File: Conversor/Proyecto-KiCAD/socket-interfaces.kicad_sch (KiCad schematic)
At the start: 24 parts, among them J7 DIMM100, P10 Header GPIO, P11 Header SD, P5 Header 7X2, P6 Header UART, P7 Header I2C, P8 Header PWM, P9 Header ADC, SW1 Switch, SW2 Switch, SW3 Switch, SW4 Switch

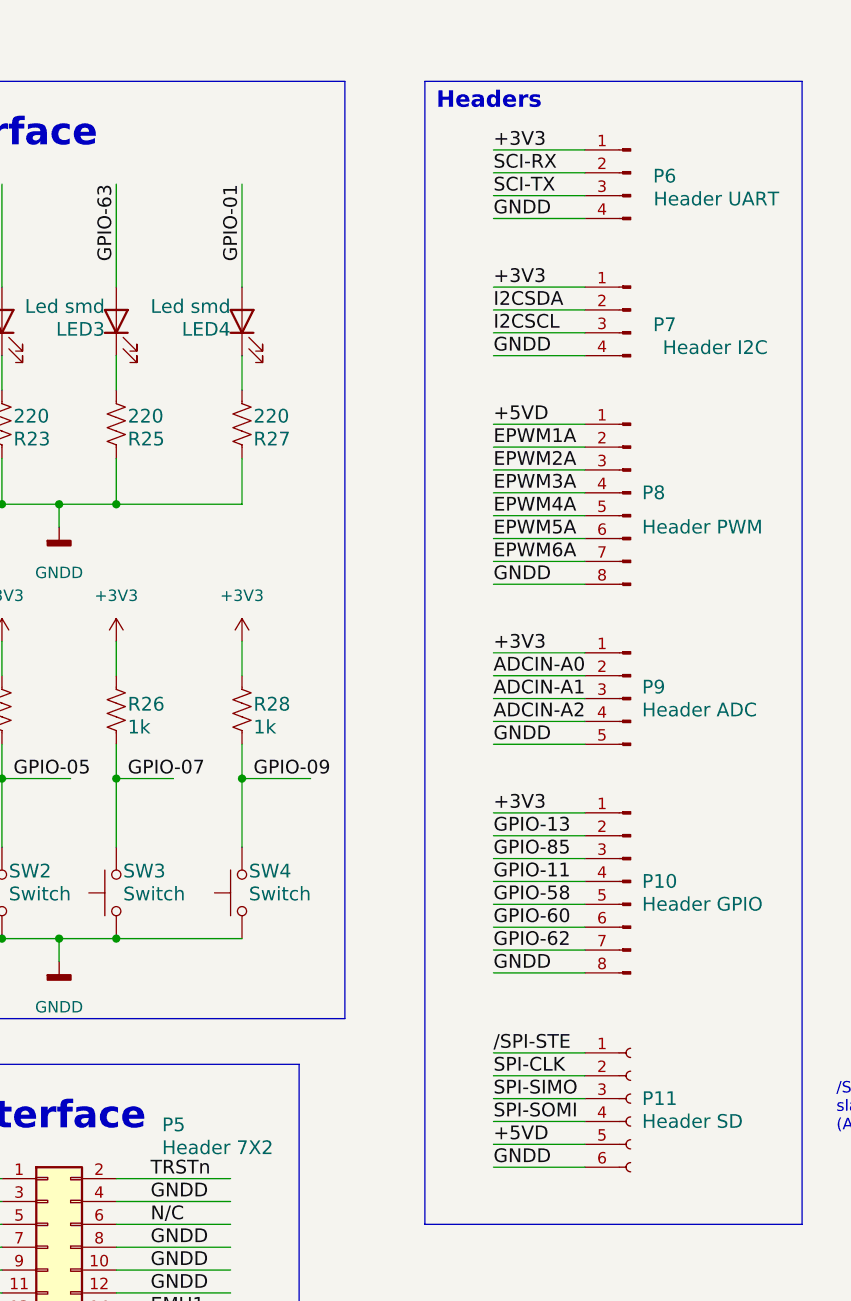
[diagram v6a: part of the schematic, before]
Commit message: Agregar el selector de alim. de 12V y seguir emprolijando la placa
- Agregar modelos de los switches
- Agregar algunos test points
Por hacer:
  - Todo lo de los dos anteriores commits
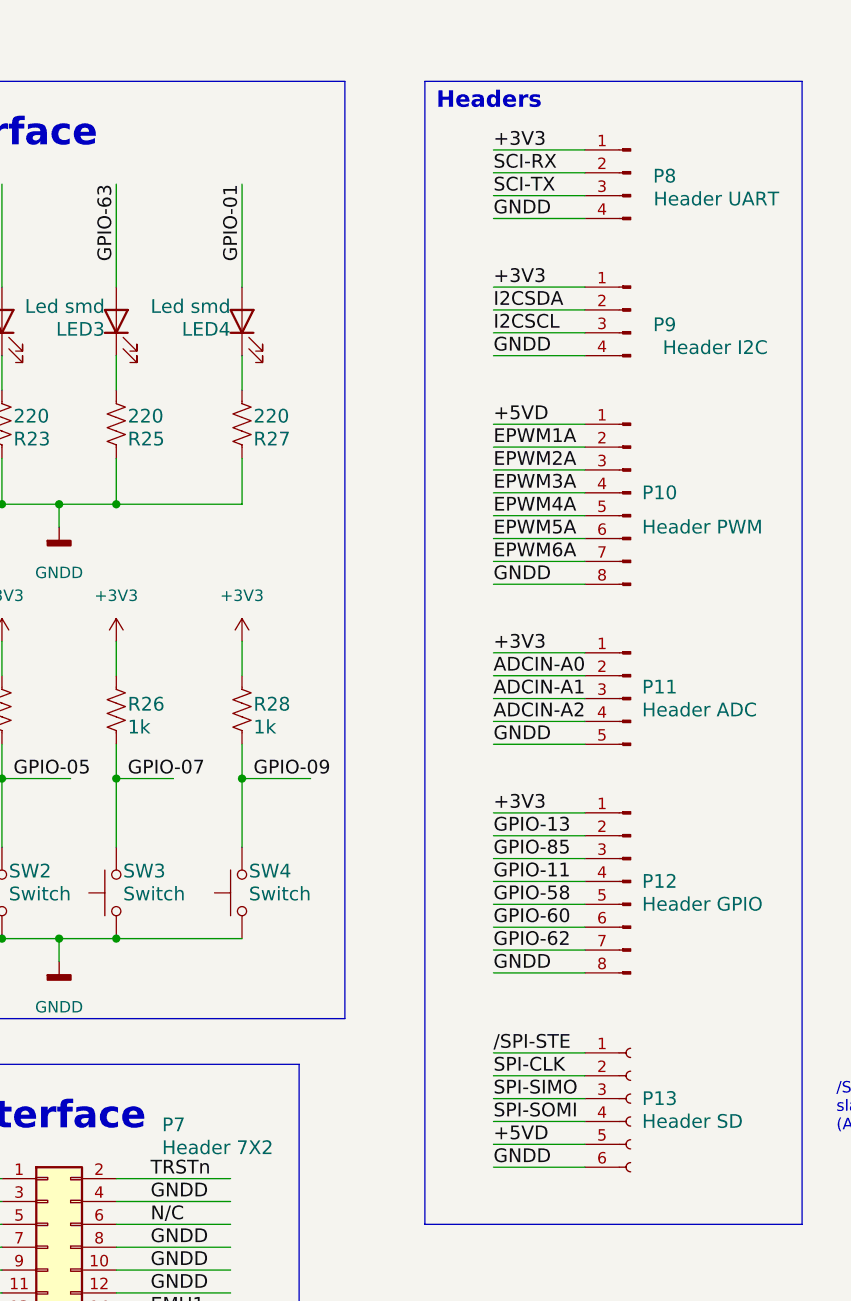
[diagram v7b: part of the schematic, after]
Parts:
- renumbered P8 to P10, P9 to P11, P10 to P12, P11 to P13, P5 to P7, P6 to P8, P7 to P9
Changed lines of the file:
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@@
   (symbol (lib_id "power:+3V3") (at 133.35 90.17 0) (unit 1)
     (in_bom yes) (on_board yes) (fields_autoplaced)
-    (property "Reference" "#PWR0119" (id 0) (at 133.35 93.98 0)
+    (property "Reference" "#PWR080" (id 0) (at 133.35 93.98 0)
       (effects (font (size 1.27 1.27)) hide)
     )
@@
   (symbol (lib_id "power:+3V3") (at 120.65 90.17 0) (unit 1)
     (in_bom yes) (on_board yes) (fields_autoplaced)
-    (property "Reference" "#PWR0144" (id 0) (at 120.65 93.98 0)
+    (property "Reference" "#PWR077" (id 0) (at 120.65 93.98 0)
       (effects (font (size 1.27 1.27)) hide)
     )
@@
   (symbol (lib_id "Connector:Conn_01x04_Male") (at 190.5 38.1 0) (mirror y) (unit 1)
     (in_bom yes) (on_board yes)
-    (property "Reference" "P6" (id 0) (at 195.58 39.37 0)
+    (property "Reference" "P8" (id 0) (at 195.58 39.37 0)
       (effects (font (size 1.524 1.524)) (justify left bottom))
     )
@@
   (symbol (lib_id "Connector_Generic:Conn_02x07_Odd_Even") (at 125.73 157.48 0) (unit 1)
     (in_bom yes) (on_board yes)
-    (property "Reference" "P5" (id 0) (at 138.43 144.78 0)
+    (property "Reference" "P7" (id 0) (at 138.43 144.78 0)
       (effects (font (size 1.524 1.524)) (justify left bottom))
     )
@@
   (symbol (lib_id "power:+3V3") (at 147.32 90.17 0) (unit 1)
     (in_bom yes) (on_board yes) (fields_autoplaced)
-    (property "Reference" "#PWR0121" (id 0) (at 147.32 93.98 0)
+    (property "Reference" "#PWR081" (id 0) (at 147.32 93.98 0)
       (effects (font (size 1.27 1.27)) hide)
     )
@@
   (symbol (lib_id "Connector:Conn_01x04_Male") (at 190.5 53.34 0) (mirror y) (unit 1)
     (in_bom yes) (on_board yes)
-    (property "Reference" "P7" (id 0) (at 195.58 55.88 0)
+    (property "Reference" "P9" (id 0) (at 195.58 55.88 0)
       (effects (font (size 1.524 1.524)) (justify left bottom))
     )
@@
   (symbol (lib_id "Connector:Conn_01x06_Female") (at 190.5 140.97 0) (unit 1)
     (in_bom yes) (on_board yes)
-    (property "Reference" "P11" (id 0) (at 191.77 140.97 0)
+    (property "Reference" "P13" (id 0) (at 191.77 140.97 0)
       (effects (font (size 1.524 1.524)) (justify left))
     )
@@
   (symbol (lib_id "power:GNDD") (at 127 77.47 0) (unit 1)
     (in_bom yes) (on_board yes) (fields_autoplaced)
-    (property "Reference" "#PWR0120" (id 0) (at 127 83.82 0)
+    (property "Reference" "#PWR078" (id 0) (at 127 83.82 0)
       (effects (font (size 1.27 1.27)) hide)
     )
@@
   (symbol (lib_id "Connector:Conn_01x05_Male") (at 190.5 96.52 0) (mirror y) (unit 1)
     (in_bom yes) (on_board yes)
-    (property "Reference" "P9" (id 0) (at 191.77 95.25 0)
+    (property "Reference" "P11" (id 0) (at 191.77 95.25 0)
       (effects (font (size 1.524 1.524)) (justify right))
     )
@@
   (symbol (lib_id "Connector:Conn_01x08_Male") (at 190.5 116.84 0) (mirror y) (unit 1)
     (in_bom yes) (on_board yes)
-    (property "Reference" "P10" (id 0) (at 191.77 116.84 0)
+    (property "Reference" "P12" (id 0) (at 191.77 116.84 0)
       (effects (font (size 1.524 1.524)) (justify right))
     )
@@
   (symbol (lib_id "power:+5VD") (at 251.46 36.83 0) (unit 1)
     (in_bom yes) (on_board yes) (fields_autoplaced)
-    (property "Reference" "#PWR0115" (id 0) (at 251.46 40.64 0)
+    (property "Reference" "#PWR082" (id 0) (at 251.46 40.64 0)
       (effects (font (size 1.27 1.27)) hide)
     )
@@
   (symbol (lib_id "power:GNDD") (at 264.16 40.64 0) (unit 1)
     (in_bom yes) (on_board yes) (fields_autoplaced)
-    (property "Reference" "#PWR0117" (id 0) (at 264.16 46.99 0)
+    (property "Reference" "#PWR084" (id 0) (at 264.16 46.99 0)
       (effects (font (size 1.27 1.27)) hide)
     )
@@
   (symbol (lib_id "power:+3V3") (at 106.68 90.17 0) (unit 1)
     (in_bom yes) (on_board yes) (fields_autoplaced)
-    (property "Reference" "#PWR0122" (id 0) (at 106.68 93.98 0)
+    (property "Reference" "#PWR076" (id 0) (at 106.68 93.98 0)
       (effects (font (size 1.27 1.27)) hide)
     )
@@
   (symbol (lib_id "power:+3V3") (at 257.81 36.83 0) (unit 1)
     (in_bom yes) (on_board yes) (fields_autoplaced)
-    (property "Reference" "#PWR0118" (id 0) (at 257.81 40.64 0)
+    (property "Reference" "#PWR083" (id 0) (at 257.81 40.64 0)
       (effects (font (size 1.27 1.27)) hide)
     )
@@
   (symbol (lib_id "Connector:Conn_01x08_Male") (at 190.5 73.66 0) (mirror y) (unit 1)
     (in_bom yes) (on_board yes) (fields_autoplaced)
-    (property "Reference" "P8" (id 0) (at 191.77 73.66 0)
+    (property "Reference" "P10" (id 0) (at 191.77 73.66 0)
       (effects (font (size 1.524 1.524)) (justify right))
     )
@@
   (symbol (lib_id "power:GNDD") (at 127 125.73 0) (unit 1)
     (in_bom yes) (on_board yes) (fields_autoplaced)
-    (property "Reference" "#PWR0123" (id 0) (at 127 132.08 0)
-      (effects (font (size 1.27 1.27)) hide)
-    )
+    (property "Reference" "#PWR079" (id 0) (at 127 132.08 0)
+      (effects (font (size 1.27 1.27)) hide)
+    )

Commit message: Commit para escribir que habría que hacer
- Mantener el ancho de las pistas de alimentación constante
- Ver las layout recommendation de todos los reguladores y resto de los
integrados
- Ver de hacer la footprint de la resistencia shunt con dos pads
separados como esta en la hoja de datos
- Falta ver el espacio para disipadores y las correcciones de Jorge
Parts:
- P8: footprint Connector_PinHeader_2.54mm:PinHeader_1x04_P2.54mm_Vertical -> Connector_PinSocket_2.54mm:PinSocket_1x04_P2.54mm_Vertical
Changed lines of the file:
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@@
       (effects (font (size 1.524 1.524)) (justify left bottom))
     )
-    (property "Footprint" "Connector_PinHeader_2.54mm:PinHeader_1x04_P2.54mm_Vertical" (id 2) (at 190.5 38.1 0)
+    (property "Footprint" "Connector_PinSocket_2.54mm:PinSocket_1x04_P2.54mm_Vertical" (id 2) (at 190.5 38.1 0)
       (effects (font (size 1.27 1.27)) hide)
     )
